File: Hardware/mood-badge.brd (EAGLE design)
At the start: 76.2 x 101.6 mm, 92 parts

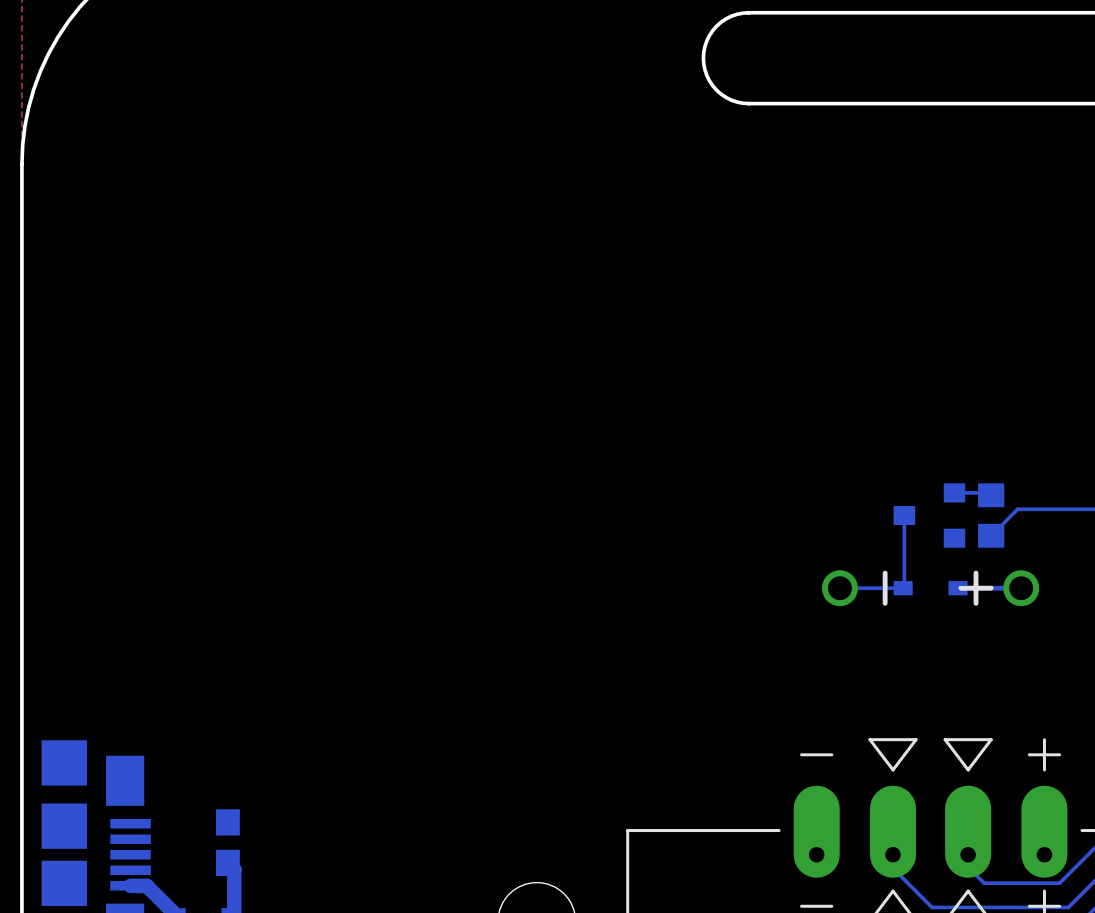
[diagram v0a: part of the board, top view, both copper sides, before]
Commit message: Name/contact/revision on PCB
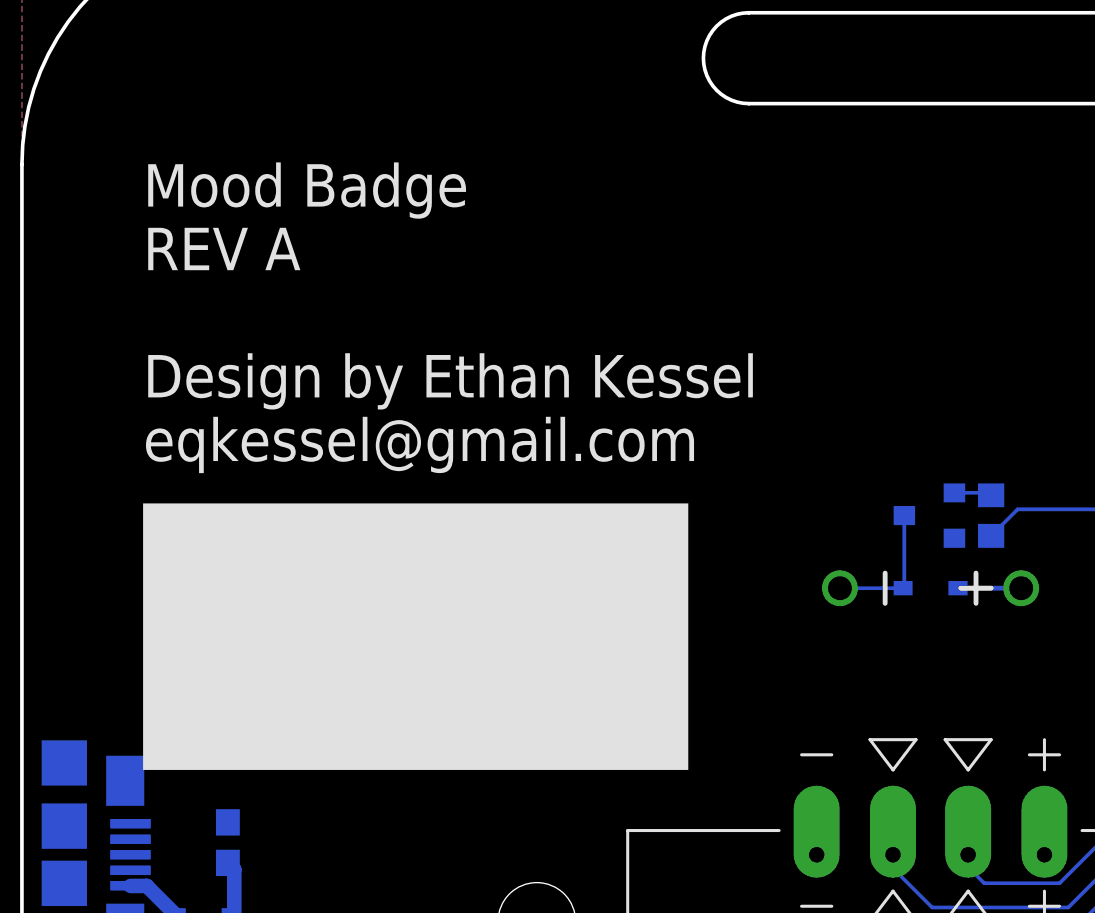
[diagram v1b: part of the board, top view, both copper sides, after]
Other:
- board text added: "Mood Badge REV A Design by Ethan Kessel eqkessel@gmail.com"
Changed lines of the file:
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@@
 <wire x1="10.16" y1="101.6" x2="0" y2="91.44" width="0.1524" layer="20" curve="90" locked="yes"/>
 <wire x1="0" y1="91.44" x2="0" y2="10.16" width="0.1524" layer="20" locked="yes"/>
+<text x="5.08" y="91.44" size="1.778" layer="21" align="top-left">Mood Badge
+REV A
+Design by Ethan Kessel
+eqkessel@gmail.com</text>
+<rectangle x1="5.08" y1="66.04" x2="27.94" y2="77.216" layer="21"/>
 </plain>
 <attributes>
@@
 <wire x1="68.389" y1="82.22" x2="68.389" y2="85.42" width="0" layer="19" extent="1-1"/>
 <wire x1="62.444" y1="82.22" x2="68.389" y2="82.22" width="0" layer="19" extent="1-1"/>
-<wire x1="56.896" y1="80.772" x2="62.444" y2="82.22" width="0" layer="19" extent="1-1"/>
-<wire x1="59.436" y1="76.034" x2="56.896" y2="79.617" width="0" layer="19" extent="1-16"/>
-<wire x1="60.96" y1="76.034" x2="59.436" y2="76.034" width="0" layer="19" extent="16-16"/>
-<wire x1="56.6166" y1="74.86" x2="59.436" y2="76.034" width="0" layer="19" extent="16-16"/>
-<wire x1="56.6166" y1="73.26" x2="56.6166" y2="74.86" width="0" layer="19" extent="16-16"/>
-<wire x1="62.318" y1="71.628" x2="60.96" y2="76.034" width="0" layer="19" extent="16-16"/>
-<wire x1="62.318" y1="70.104" x2="62.318" y2="71.628" width="0" layer="19" extent="16-16"/>
-<wire x1="73.152" y1="77.47" x2="68.389" y2="82.22" width="0" layer="19" extent="1-1"/>
-<wire x1="73.152" y1="74.93" x2="73.152" y2="77.47" width="0" layer="19" extent="1-1"/>
-<wire x1="70.866" y1="69.596" x2="73.152" y2="74.93" width="0" layer="19" extent="1-1"/>
-<wire x1="70.612" y1="61.302" x2="70.866" y2="69.596" width="0" layer="19" extent="16-16"/>
-<wire x1="68.58" y1="61.302" x2="70.612" y2="61.302" width="0" layer="19" extent="16-16"/>
-<wire x1="64.2319" y1="60.452" x2="68.58" y2="61.302" width="0" layer="19" extent="16-16"/>
-<wire x1="64.008" y1="55.03" x2="64.2319" y2="60.452" width="0" layer="19" extent="16-16"/>
-<wire x1="68.58" y1="53.174" x2="64.008" y2="55.03" width="0" layer="19" extent="16-16"/>
-<wire x1="68.58" y1="49.618" x2="68.58" y2="53.174" width="0" layer="19" extent="16-16"/>
-<wire x1="70.954" y1="46.228" x2="68.58" y2="49.618" width="0" layer="19" extent="16-16"/>
-<wire x1="63.97" y1="43.092" x2="70.954" y2="46.228" width="0" layer="19" extent="1-16"/>
-<wire x1="48.0314" y1="74.06" x2="56.6166" y2="74.86" width="0" layer="19" extent="16-16"/>
-<wire x1="39.1" y1="75.758" x2="48.0314" y2="74.06" width="0" layer="19" extent="16-16"/>
-<wire x1="54.356" y1="50.924" x2="64.008" y2="55.03" width="0" layer="19" extent="16-16"/>
-<wire x1="49.784" y1="46.0248" x2="54.356" y2="50.924" width="0" layer="19" extent="16-16"/>
-<wire x1="60.96" y1="27.774" x2="62.484" y2="41.656" width="0" layer="19" extent="1-1"/>
-<wire x1="54.356" y1="20.662" x2="59.436" y2="27.432" width="0" layer="19" extent="1-1"/>
-<wire x1="39.458" y1="18.288" x2="47.752" y2="20.32" width="0" layer="19" extent="1-1"/>
-<wire x1="25.908" y1="14.732" x2="39.458" y2="15.748" width="0" layer="19" extent="1-1"/>
-<wire x1="8.294" y1="15.748" x2="19.304" y2="15.074" width="0" layer="19" extent="1-1"/>
-<wire x1="7.256" y1="24.876" x2="8.294" y2="18.288" width="0" layer="19" extent="1-16"/>
-<wire x1="33.3248" y1="62.484" x2="39.1" y2="75.758" width="0" layer="19" extent="16-16"/>
-<wire x1="28.448" y1="33.108" x2="39.116" y2="19.812" width="0" layer="19" extent="1-1"/>
-<wire x1="33.3248" y1="39.116" x2="28.448" y2="33.108" width="0" layer="19" extent="1-1"/>
-<wire x1="18.122" y1="41.148" x2="21.844" y2="32.512" width="0" layer="19" extent="16-16"/>
-<wire x1="18.122" y1="43.18" x2="18.122" y2="41.148" width="0" layer="19" extent="16-16"/>
-<wire x1="17.106" y1="46.482" x2="18.122" y2="43.18" width="0" layer="19" extent="16-16"/>
-<wire x1="17.106" y1="48.514" x2="17.106" y2="46.482" width="0" layer="19" extent="16-16"/>
-<wire x1="16.256" y1="49.784" x2="17.106" y2="48.514" width="0" layer="19" extent="16-16"/>
-<wire x1="13.208" y1="47.11" x2="15.074" y2="49.784" width="0" layer="19" extent="1-16"/>
-<wire x1="10.922" y1="47.11" x2="13.208" y2="47.11" width="0" layer="19" extent="16-16"/>
-<wire x1="14.183" y1="44.414" x2="13.208" y2="47.11" width="0" layer="19" extent="16-16"/>
-<wire x1="12.233" y1="39.914" x2="14.183" y2="44.414" width="0" layer="19" extent="16-16"/>
-<wire x1="11.684" y1="37.426" x2="12.233" y2="39.914" width="0" layer="19" extent="16-16"/>
-<wire x1="6.096" y1="48.934" x2="10.922" y2="47.11" width="0" layer="19" extent="16-16"/>
-<wire x1="7.112" y1="54.6401" x2="6.096" y2="48.934" width="0" layer="19" extent="16-16"/>
-<wire x1="5.754" y1="57.15" x2="7.112" y2="54.6401" width="0" layer="19" extent="16-16"/>
-<wire x1="4.553" y1="63.784" x2="5.754" y2="57.15" width="0" layer="19" extent="16-16"/>
-<wire x1="8.636" y1="63.842" x2="4.553" y2="63.784" width="0" layer="19" extent="16-16"/>
-<wire x1="26.416" y1="46.0248" x2="18.122" y2="43.18" width="0" layer="19" extent="16-16"/>
 </signal>
 <signal name="N$1">
@@
 </signals>
 <mfgpreviewcolors>
-<mfgpreviewcolor name="soldermaskcolor" color="0xC8008000"/>
+<mfgpreviewcolor name="soldermaskcolor" color="0xC855007F"/>
 <mfgpreviewcolor name="silkscreencolor" color="0xFFFEFEFE"/>
 <mfgpreviewcolor name="backgroundcolor" color="0xFF282828"/>
@@
 </drawing>
 <compatibility>
+<note version="6.3" minversion="6.2.2" severity="warning">
+Since Version 6.2.2 text objects can contain more than one line,
+which will not be processed correctly with this version.
+</note>
 <note version="8.3" severity="warning">
 Since Version 8.3, EAGLE supports Fusion synchronisation.

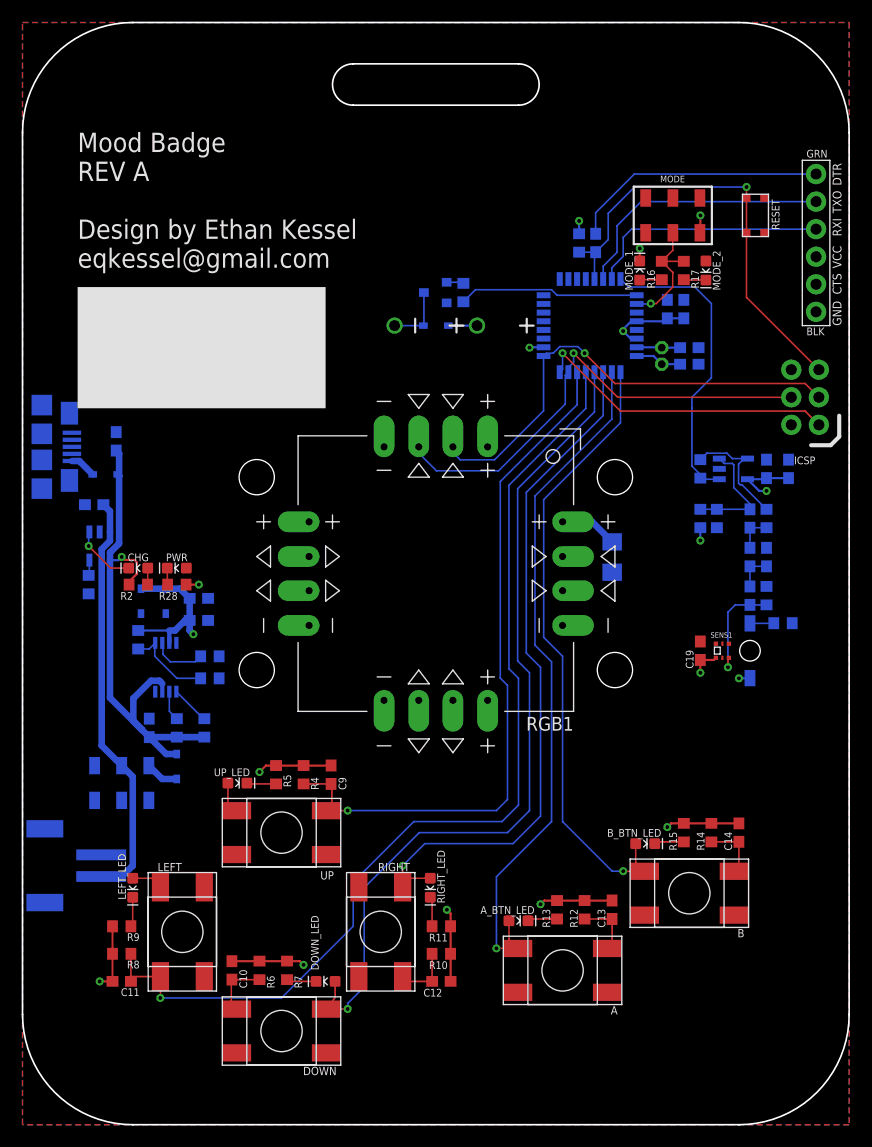
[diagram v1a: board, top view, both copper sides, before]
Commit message: Minor fixes and routing changes
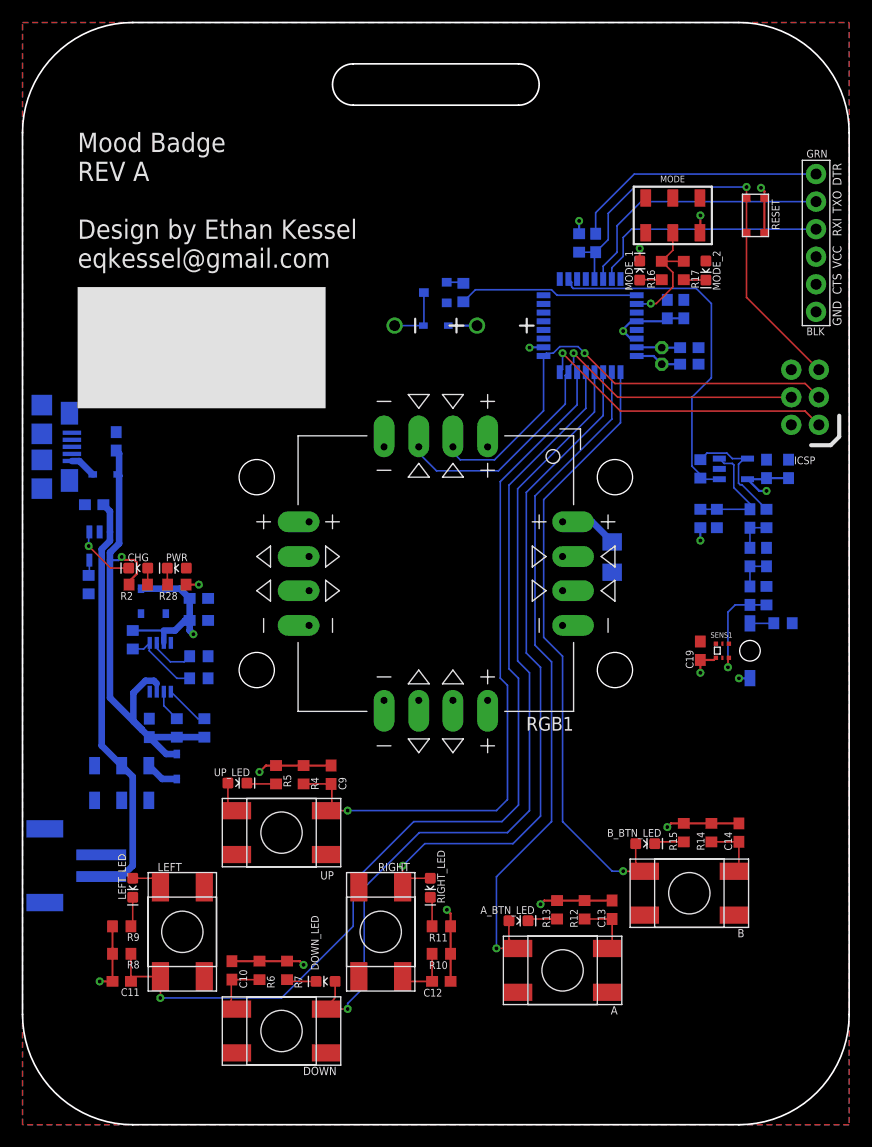
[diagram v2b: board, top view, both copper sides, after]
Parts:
- moved R25 1.02 mm to (16.3, 43.2)
- moved R26 1.02 mm to (16.3, 41.1)
- moved BOOST 0.51 mm to (12.7, 42.2)
- moved R27 0.51 mm to (10.2, 44.7)
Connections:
- net PULSE: now also ARDUINO.26; no longer ARDUINO.32
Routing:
- net PULSE: track 28.3 -> 33.3 mm
- net GND: track 47.7 -> 52.0 mm, vias 10 -> 11
- net N$30: track 8.12 -> 7.31 mm
- net N$27: track 5.06 -> 4.25 mm
- net VCC: track 41.1 -> 41.6 mm
- net N$29: track 3.61 -> 4.12 mm
